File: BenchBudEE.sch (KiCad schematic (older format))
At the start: 0 parts

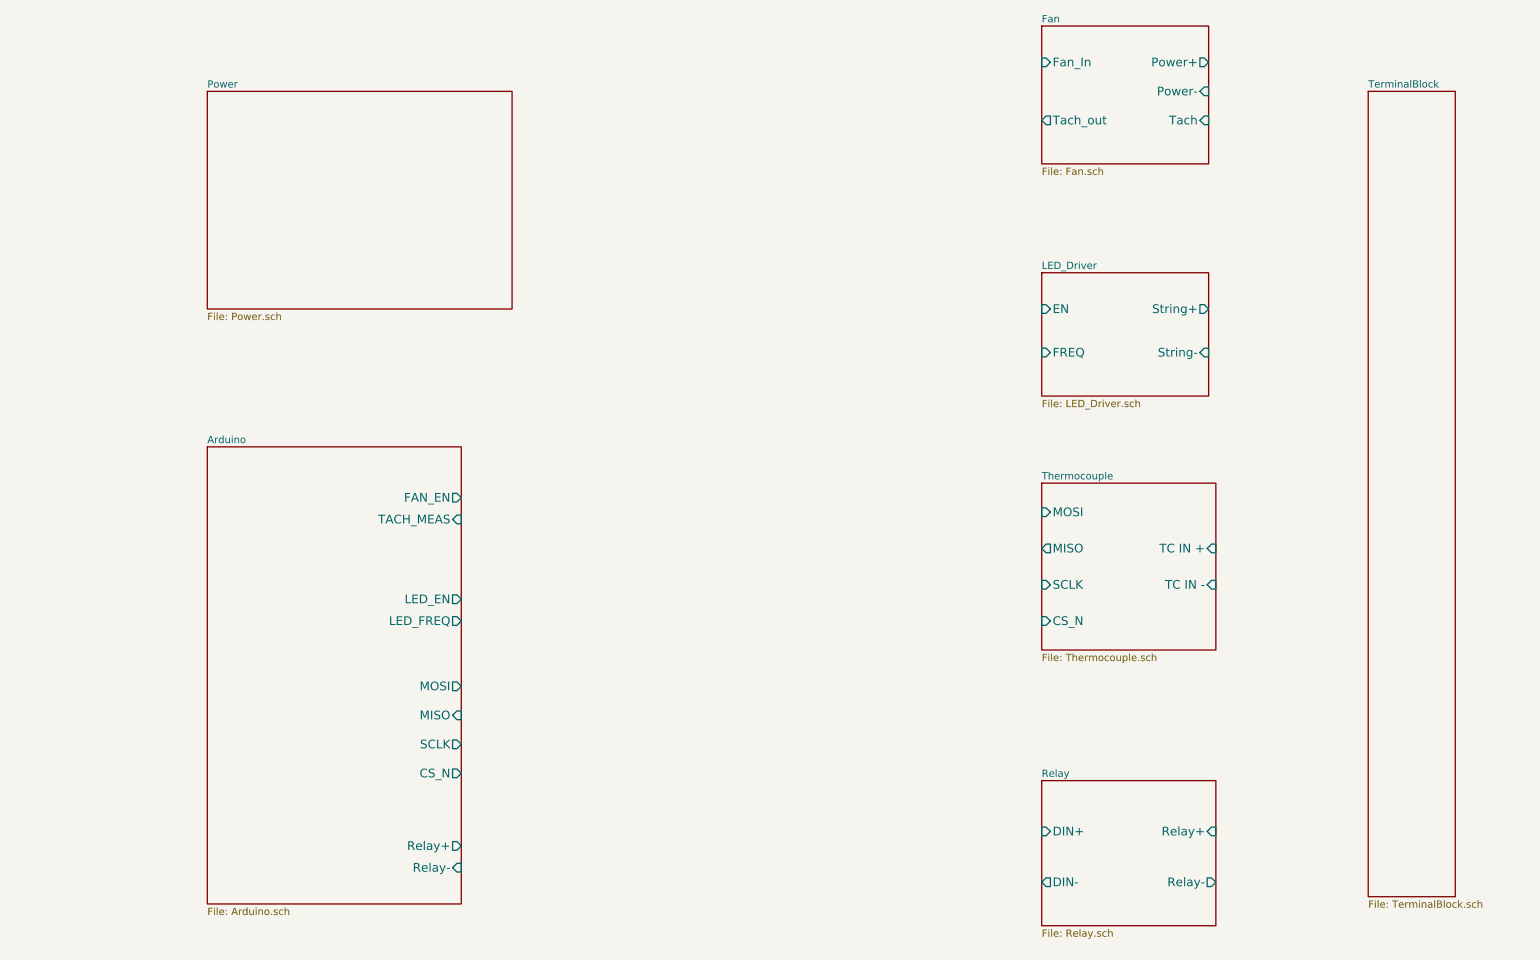
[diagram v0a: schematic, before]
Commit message: Created CurrentDriver, Relay, and PowerProtection modules
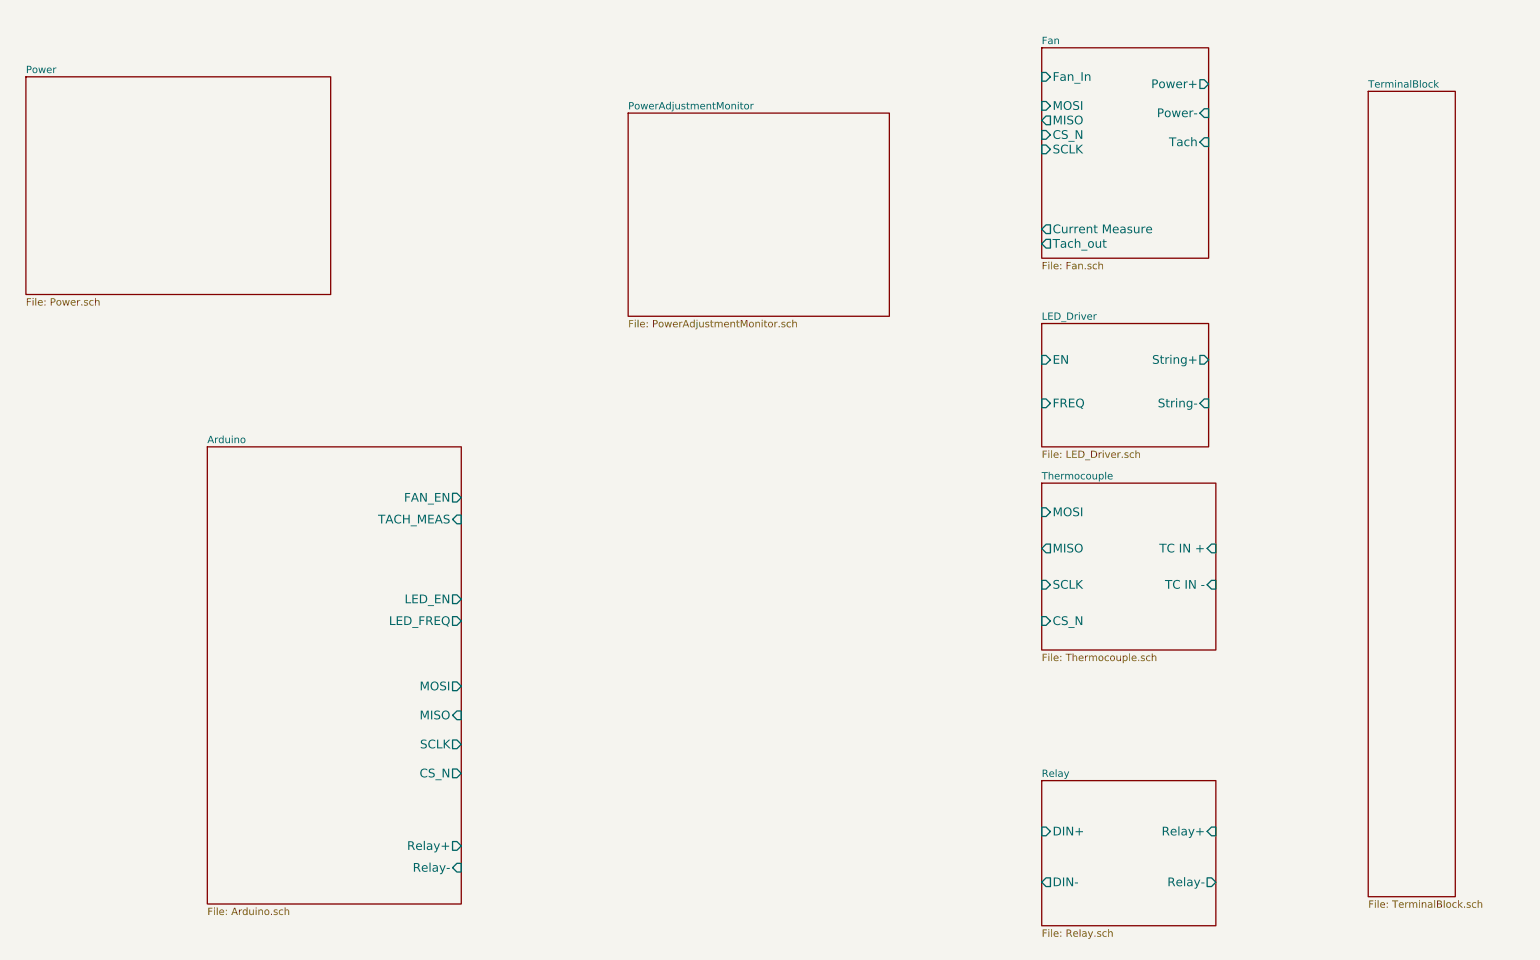
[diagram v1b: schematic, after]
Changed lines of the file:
@@
 LIBS:contrib
 LIBS:valves
+LIBS:BenchBudEE
 LIBS:BenchBudEE-cache
 EELAYER 27 0
@@
 $Descr A4 11693 8268
 encoding utf-8
-Sheet 1 8
+Sheet 1 9
 Title ""
-Date "6 feb 2014"
+Date "9 feb 2014"
 Rev ""
 Comp ""
@@
 $EndSheet
 $Sheet
-S 2450 1200 2100 1500
+S 1200 1100 2100 1500
 U 52F2E422
 F0 "Power" 50
 F1 "Power.sch" 50
-$EndSheet
-$Sheet
-S 8200 750  1150 950
-U 52F2E477
-F0 "Fan" 50
-F1 "Fan.sch" 50
-F2 "Power+" O R 9350 1000 60
-F3 "Power-" I R 9350 1200 60
-F4 "Tach" I R 9350 1400 60
-F5 "Tach_out" O L 8200 1400 60
-F6 "Fan_In" I L 8200 1000 60
 $EndSheet
 $Sheet
@@
 $EndSheet
 $Sheet
-S 8200 2450 1150 850
+S 8200 2800 1150 850
 U 52F2E458
 F0 "LED_Driver" 50
 F1 "LED_Driver.sch" 50
-F2 "EN" I L 8200 2700 60
-F3 "FREQ" I L 8200 3000 60
-F4 "String+" O R 9350 2700 60
-F5 "String-" I R 9350 3000 60
+F2 "EN" I L 8200 3050 60
+F3 "FREQ" I L 8200 3350 60
+F4 "String+" O R 9350 3050 60
+F5 "String-" I R 9350 3350 60
+$EndSheet
+$Sheet
+S 8200 900  1150 1450
+U 52F2E477
+F0 "Fan" 50
+F1 "Fan.sch" 50
+F2 "Power+" O R 9350 1150 60
+F3 "Power-" I R 9350 1350 60
+F4 "Tach" I R 9350 1550 60
+F5 "Tach_out" O L 8200 2250 60
+F6 "Fan_In" I L 8200 1100 60
+F7 "Current Measure" O L 8200 2150 60
+F8 "MOSI" I L 8200 1300 60
+F9 "MISO" O L 8200 1400 60
+F10 "CS_N" I L 8200 1500 60
+F11 "SCLK" I L 8200 1600 60
+$EndSheet
+$Sheet
+S 5350 1350 1800 1400
+U 52F67DEA
+F0 "PowerAdjustmentMonitor" 50
+F1 "PowerAdjustmentMonitor.sch" 50
 $EndSheet
 $EndSCHEMATC

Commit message: Current driver refactoring, LED module, Arduino
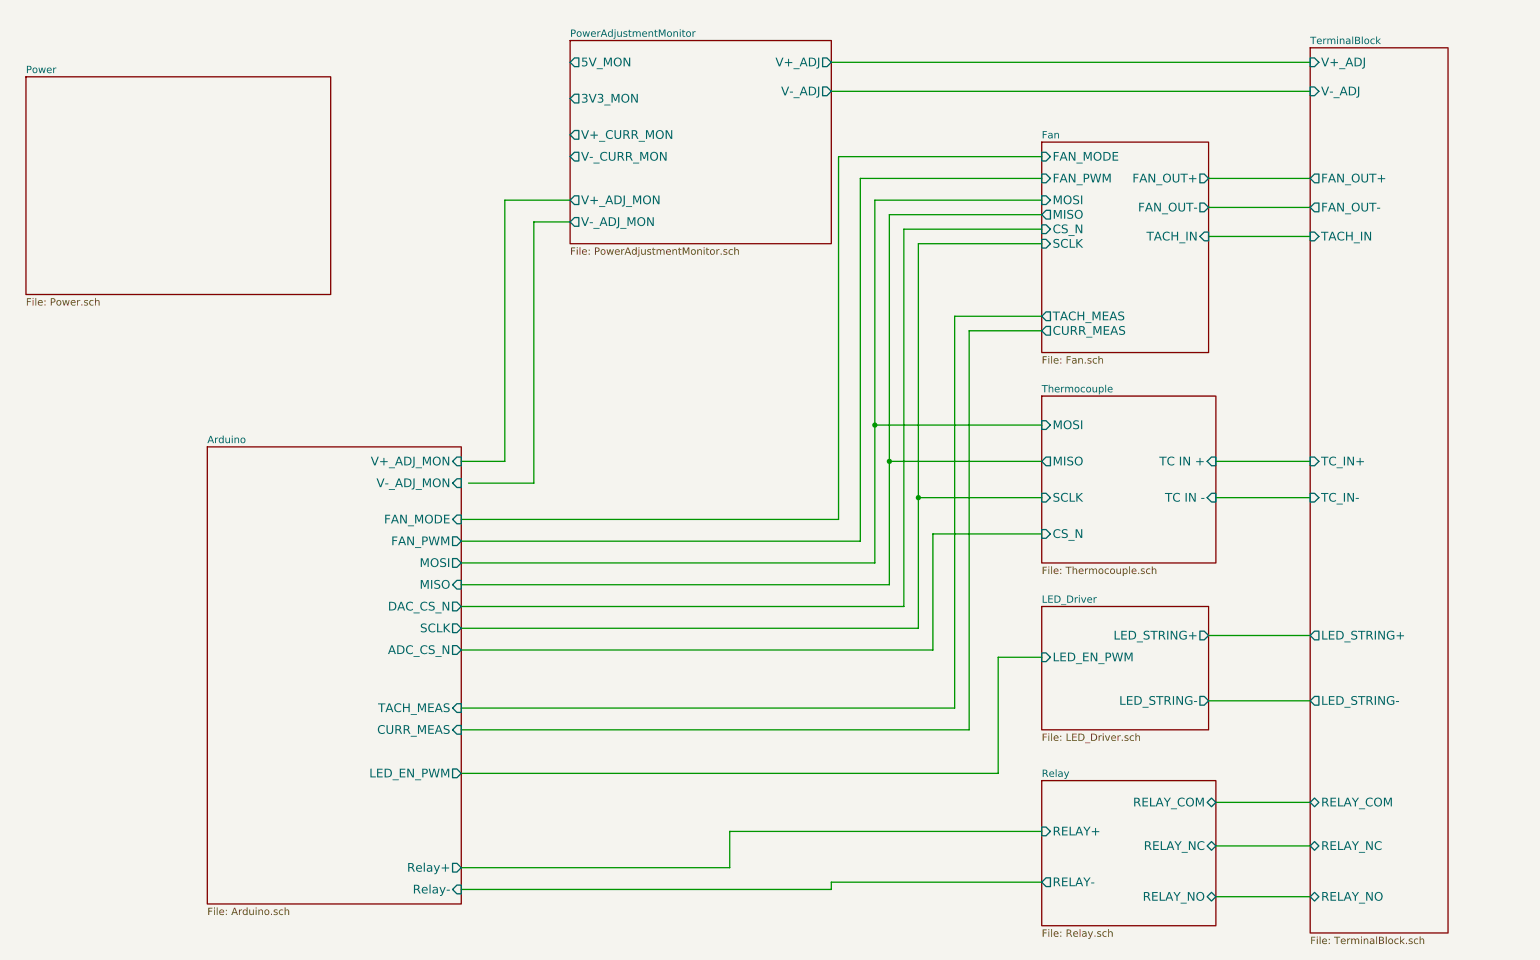
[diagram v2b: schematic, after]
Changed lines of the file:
@@
 $EndDescr
+$Sheet
+S 8200 3300 1200 1150
+U 52F2E40C
+F0 "Thermocouple" 50
+F1 "Thermocouple.sch" 50
+F2 "TC IN +" I R 9400 3750 60
+F3 "TC IN -" I R 9400 4000 60
+F4 "MOSI" I L 8200 3500 60
+F5 "MISO" O L 8200 3750 60
+F6 "SCLK" I L 8200 4000 60
+F7 "CS_N" I L 8200 4250 60
+$EndSheet
+$Sheet
+S 8200 5950 1200 1000
+U 52F2E418
+F0 "Relay" 50
+F1 "Relay.sch" 50
+F2 "RELAY_NC" B R 9400 6400 60
+F3 "RELAY_NO" B R 9400 6750 60
+F4 "RELAY_COM" B R 9400 6100 60
+F5 "RELAY+" I L 8200 6300 60
+F6 "RELAY-" O L 8200 6650 60
+$EndSheet
+$Sheet
+S 1200 1100 2100 1500
+U 52F2E422
+F0 "Power" 50
+F1 "Power.sch" 50
+$EndSheet
+$Sheet
+S 8200 4750 1150 850
+U 52F2E458
+F0 "LED_Driver" 50
+F1 "LED_Driver.sch" 50
+F2 "LED_EN_PWM" I L 8200 5100 60
+F3 "LED_STRING+" O R 9350 4950 60
+F4 "LED_STRING-" O R 9350 5400 60
+$EndSheet
+$Sheet
+S 8200 1550 1150 1450
+U 52F2E477
+F0 "Fan" 50
+F1 "Fan.sch" 50
+F2 "MOSI" I L 8200 1950 60
+F3 "MISO" O L 8200 2050 60
+F4 "CS_N" I L 8200 2150 60
+F5 "SCLK" I L 8200 2250 60
+F6 "FAN_OUT+" O R 9350 1800 60
+F7 "TACH_IN" I R 9350 2200 60
+F8 "TACH_MEAS" O L 8200 2750 60
+F9 "CURR_MEAS" O L 8200 2850 60
+F10 "FAN_OUT-" O R 9350 2000 60
+F11 "FAN_PWM" I L 8200 1800 60
+F12 "FAN_MODE" I L 8200 1650 60
+$EndSheet
+$Sheet
+S 4950 850  1800 1400
+U 52F67DEA
+F0 "PowerAdjustmentMonitor" 50
+F1 "PowerAdjustmentMonitor.sch" 50
+F2 "V+_ADJ" O R 6750 1000 60
+F3 "V-_ADJ" O R 6750 1200 60
+F4 "3V3_MON" O L 4950 1250 60
+F5 "5V_MON" O L 4950 1000 60
+F6 "V+_ADJ_MON" O L 4950 1950 60
+F7 "V-_ADJ_MON" O L 4950 2100 60
+F8 "V+_CURR_MON" O L 4950 1500 60
+F9 "V-_CURR_MON" O L 4950 1650 60
+$EndSheet
+$Sheet
+S 10050 900  950  6100
+U 52F2E4B8
+F0 "TerminalBlock" 50
+F1 "TerminalBlock.sch" 50
+F2 "V+_ADJ" I L 10050 1000 60
+F3 "V-_ADJ" I L 10050 1200 60
+F4 "FAN_OUT+" O L 10050 1800 60
+F5 "FAN_OUT-" O L 10050 2000 60
+F6 "TACH_IN" I L 10050 2200 60
+F7 "RELAY_COM" B L 10050 6100 60
+F8 "RELAY_NO" B L 10050 6750 60
+F9 "RELAY_NC" B L 10050 6400 60
+F10 "LED_STRING+" O L 10050 4950 60
+F11 "LED_STRING-" O L 10050 5400 60
+F12 "TC_IN+" I L 10050 3750 60
+F13 "TC_IN-" I L 10050 4000 60
+$EndSheet
+Wire Wire Line
+	9400 6100 10050 6100
+Wire Wire Line
+	9400 6400 10050 6400
+Wire Wire Line
+	9400 6750 10050 6750
+Wire Wire Line
+	9350 2200 10050 2200
+Wire Wire Line
+	9350 2000 10050 2000
+Wire Wire Line
+	9350 1800 10050 1800
+Wire Wire Line
+	6750 1000 10050 1000
+Wire Wire Line
+	10050 1200 6750 1200
+Wire Wire Line
+	4200 3750 4500 3750
+Wire Wire Line
+	4500 3750 4500 1950
+Wire Wire Line
+	4500 1950 4950 1950
+Wire Wire Line
+	4250 3900 4700 3900
+Wire Wire Line
+	4700 3900 4700 2100
+Wire Wire Line
+	4700 2100 4950 2100
+Wire Wire Line
+	4200 4300 6950 4300
+Wire Wire Line
+	6950 4300 6950 1800
+Wire Wire Line
+	6950 1800 8200 1800
+Wire Wire Line
+	7050 4450 4200 4450
+Wire Wire Line
+	7050 1950 7050 4450
+Wire Wire Line
+	7050 1950 8200 1950
+Wire Wire Line
+	7150 4600 4200 4600
+Wire Wire Line
+	7150 2050 7150 4600
+Wire Wire Line
+	7150 2050 8200 2050
+Wire Wire Line
+	4200 4750 7250 4750
+Wire Wire Line
+	7250 4750 7250 2150
+Wire Wire Line
+	7250 2150 8200 2150
+Wire Wire Line
+	7350 4900 4200 4900
+Wire Wire Line
+	7350 2250 7350 4900
+Wire Wire Line
+	7350 2250 8200 2250
+Wire Wire Line
+	9400 3750 10050 3750
+Wire Wire Line
+	10050 4000 9400 4000
+Wire Wire Line
+	9350 4950 10050 4950
+Wire Wire Line
+	10050 5400 9350 5400
+Wire Wire Line
+	8200 3500 7050 3500
+Connection ~ 7050 3500
+Wire Wire Line
+	8200 3750 7150 3750
+Connection ~ 7150 3750
+Wire Wire Line
+	8200 4000 7350 4000
+Connection ~ 7350 4000
+Wire Wire Line
+	4200 5050 7450 5050
+Wire Wire Line
+	7450 5050 7450 4250
+Wire Wire Line
+	7450 4250 8200 4250
 $Sheet
 S 2450 3650 1750 3150
@@
 F0 "Arduino" 50
 F1 "Arduino.sch" 50
-F2 "Relay+" O R 4200 6400 60
-F3 "Relay-" I R 4200 6550 60
-F4 "MOSI" O R 4200 5300 60
-F5 "MISO" I R 4200 5500 60
-F6 "SCLK" O R 4200 5700 60
-F7 "CS_N" O R 4200 5900 60
-F8 "LED_EN" O R 4200 4700 60
-F9 "LED_FREQ" O R 4200 4850 60
-F10 "FAN_EN" O R 4200 4000 60
-F11 "TACH_MEAS" I R 4200 4150 60
-$EndSheet
-$Sheet
-S 8200 3900 1200 1150
-U 52F2E40C
-F0 "Thermocouple" 50
-F1 "Thermocouple.sch" 50
-F2 "TC IN +" I R 9400 4350 60
-F3 "TC IN -" I R 9400 4600 60
-F4 "MOSI" I L 8200 4100 60
-F5 "MISO" O L 8200 4350 60
-F6 "SCLK" I L 8200 4600 60
-F7 "CS_N" I L 8200 4850 60
-$EndSheet
-$Sheet
-S 8200 5950 1200 1000
-U 52F2E418
-F0 "Relay" 50
-F1 "Relay.sch" 50
-F2 "DIN+" I L 8200 6300 60
-F3 "DIN-" O L 8200 6650 60
-F4 "Relay+" I R 9400 6300 60
-F5 "Relay-" O R 9400 6650 60
-$EndSheet
-$Sheet
-S 1200 1100 2100 1500
-U 52F2E422
-F0 "Power" 50
-F1 "Power.sch" 50
-$EndSheet
-$Sheet
-S 10450 1200 600  5550
-U 52F2E4B8
-F0 "TerminalBlock" 50
-F1 "TerminalBlock.sch" 50
-$EndSheet
-$Sheet
-S 8200 2800 1150 850
-U 52F2E458
-F0 "LED_Driver" 50
-F1 "LED_Driver.sch" 50
-F2 "EN" I L 8200 3050 60
-F3 "FREQ" I L 8200 3350 60
-F4 "String+" O R 9350 3050 60
-F5 "String-" I R 9350 3350 60
-$EndSheet
-$Sheet
-S 8200 900  1150 1450
-U 52F2E477
-F0 "Fan" 50
-F1 "Fan.sch" 50
-F2 "Power+" O R 9350 1150 60
-F3 "Power-" I R 9350 1350 60
-F4 "Tach" I R 9350 1550 60
-F5 "Tach_out" O L 8200 2250 60
-F6 "Fan_In" I L 8200 1100 60
-F7 "Current Measure" O L 8200 2150 60
-F8 "MOSI" I L 8200 1300 60
-F9 "MISO" O L 8200 1400 60
-F10 "CS_N" I L 8200 1500 60
-F11 "SCLK" I L 8200 1600 60
-$EndSheet
-$Sheet
-S 5350 1350 1800 1400
-U 52F67DEA
-F0 "PowerAdjustmentMonitor" 50
-F1 "PowerAdjustmentMonitor.sch" 50
-$EndSheet
+F2 "Relay+" O R 4200 6550 60
+F3 "Relay-" I R 4200 6700 60
+F4 "V+_ADJ_MON" I R 4200 3750 60
+F5 "V-_ADJ_MON" I R 4200 3900 60
+F6 "MOSI" O R 4200 4450 60
+F7 "MISO" I R 4200 4600 60
+F8 "SCLK" O R 4200 4900 60
+F9 "TACH_MEAS" I R 4200 5450 60
+F10 "CURR_MEAS" I R 4200 5600 60
+F11 "LED_EN_PWM" O R 4200 5900 60
+F12 "DAC_CS_N" O R 4200 4750 60
+F13 "ADC_CS_N" O R 4200 5050 60
+F14 "FAN_PWM" O R 4200 4300 60
+F15 "FAN_MODE" I R 4200 4150 60
+$EndSheet
+Wire Wire Line
+	4200 5450 7600 5450
+Wire Wire Line
+	7600 5450 7600 2750
+Wire Wire Line
+	7600 2750 8200 2750
+Wire Wire Line
+	8200 2850 7700 2850
+Wire Wire Line
+	7700 2850 7700 5600
+Wire Wire Line
+	7700 5600 4200 5600
+Wire Wire Line
+	4200 5900 7900 5900
+Wire Wire Line
+	7900 5900 7900 5100
+Wire Wire Line
+	7900 5100 8200 5100
+Wire Wire Line
+	4200 6550 6050 6550
+Wire Wire Line
+	6050 6550 6050 6300
+Wire Wire Line
+	6050 6300 8200 6300
+Wire Wire Line
+	4200 6700 6750 6700
+Wire Wire Line
+	6750 6700 6750 6650
+Wire Wire Line
+	6750 6650 8200 6650
+Wire Wire Line
+	8200 1650 6800 1650
+Wire Wire Line
+	6800 1650 6800 4150
+Wire Wire Line
+	6800 4150 4200 4150
 $EndSCHEMATC

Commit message: Refactoring and Created key shortcuts
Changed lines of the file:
@@
 Sheet 1 9
 Title ""
-Date "9 feb 2014"
+Date "18 feb 2014"
 Rev ""
 Comp ""
@@
 F6 "SCLK" I L 8200 4000 60
 F7 "CS_N" I L 8200 4250 60
-$EndSheet
-$Sheet
-S 8200 5950 1200 1000
-U 52F2E418
-F0 "Relay" 50
-F1 "Relay.sch" 50
-F2 "RELAY_NC" B R 9400 6400 60
-F3 "RELAY_NO" B R 9400 6750 60
-F4 "RELAY_COM" B R 9400 6100 60
-F5 "RELAY+" I L 8200 6300 60
-F6 "RELAY-" O L 8200 6650 60
 $EndSheet
 $Sheet
@@
 F6 "V+_ADJ_MON" O L 4950 1950 60
 F7 "V-_ADJ_MON" O L 4950 2100 60
-F8 "V+_CURR_MON" O L 4950 1500 60
-F9 "V-_CURR_MON" O L 4950 1650 60
 $EndSheet
 $Sheet
@@
 F5 "FAN_OUT-" O L 10050 2000 60
 F6 "TACH_IN" I L 10050 2200 60
-F7 "RELAY_COM" B L 10050 6100 60
-F8 "RELAY_NO" B L 10050 6750 60
-F9 "RELAY_NC" B L 10050 6400 60
+F7 "RELAY_COM" B L 10050 6150 60
+F8 "RELAY_NO" B L 10050 6800 60
+F9 "RELAY_NC" B L 10050 6450 60
 F10 "LED_STRING+" O L 10050 4950 60
 F11 "LED_STRING-" O L 10050 5400 60
@@
 $EndSheet
 Wire Wire Line
-	9400 6100 10050 6100
-Wire Wire Line
-	9400 6400 10050 6400
-Wire Wire Line
-	9400 6750 10050 6750
+	9400 6150 10050 6150
+Wire Wire Line
+	9400 6450 10050 6450
+Wire Wire Line
+	9400 6800 10050 6800
 Wire Wire Line
 	9350 2200 10050 2200
@@
 	4500 1950 4950 1950
 Wire Wire Line
-	4250 3900 4700 3900
+	4200 3900 4700 3900
 Wire Wire Line
 	4700 3900 4700 2100
@@
 	7050 4450 4200 4450
 Wire Wire Line
-	7050 1950 7050 4450
+	7050 1950 7050 3500
+Wire Wire Line
+	7050 3500 7050 4450
 Wire Wire Line
 	7050 1950 8200 1950
@@
 	7150 4600 4200 4600
 Wire Wire Line
-	7150 2050 7150 4600
+	7150 2050 7150 3750
+Wire Wire Line
+	7150 3750 7150 4600
 Wire Wire Line
 	7150 2050 8200 2050
@@
 	7350 4900 4200 4900
 Wire Wire Line
-	7350 2250 7350 4900
+	7350 2250 7350 4000
+Wire Wire Line
+	7350 4000 7350 4900
 Wire Wire Line
 	7350 2250 8200 2250
@@
 	4200 6550 6050 6550
 Wire Wire Line
-	6050 6550 6050 6300
-Wire Wire Line
-	6050 6300 8200 6300
+	6050 6550 6050 6350
+Wire Wire Line
+	6050 6350 8200 6350
 Wire Wire Line
 	4200 6700 6750 6700
 Wire Wire Line
-	6750 6700 6750 6650
-Wire Wire Line
-	6750 6650 8200 6650
+	6750 6700 6750 6700
+Wire Wire Line
+	6750 6700 8200 6700
 Wire Wire Line
 	8200 1650 6800 1650
@@
 Wire Wire Line
 	6800 4150 4200 4150
+$Sheet
+S 8200 6000 1200 1000
+U 52F2E418
+F0 "Relay" 50
+F1 "Relay.sch" 50
+F2 "RELAY_NC" B R 9400 6450 60
+F3 "RELAY_NO" B R 9400 6800 60
+F4 "RELAY_COM" B R 9400 6150 60
+F5 "RELAY+" I L 8200 6350 60
+F6 "RELAY-" O L 8200 6700 60
+$EndSheet
 $EndSCHEMATC
